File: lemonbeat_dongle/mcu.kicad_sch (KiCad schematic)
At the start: 39 parts, among them J201 USB_A, J202 Prog, J203 u.FL, SW201 SW_Push, U201 nRF52840, Y201 32MHz, Y202 32.768kHz

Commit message: dongle: re-add 32kHz crystal to BOM
Should not be needed, but may need software adaptation for Si4467 to
work with HFCLK, so easier to keep initially and remove later.
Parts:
- C203, C204, Y202: now in the parts list
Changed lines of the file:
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@@
   )
   (symbol (lib_id "Device:C") (at 151.13 60.96 90) (unit 1)
-    (in_bom no) (on_board yes)
+    (in_bom yes) (on_board yes)
     (property "Reference" "C204" (id 0) (at 151.13 57.15 90))
     (property "Value" "12pF" (id 1) (at 151.13 64.77 90))
@@
   )
   (symbol (lib_id "Device:C") (at 151.13 50.8 270) (unit 1)
-    (in_bom no) (on_board yes)
+    (in_bom yes) (on_board yes)
     (property "Reference" "C203" (id 0) (at 151.13 46.99 90))
     (property "Value" "12pF" (id 1) (at 151.13 54.61 90))
@@
   )
   (symbol (lib_id "Device:Crystal") (at 133.35 55.88 90) (unit 1)
-    (in_bom no) (on_board yes) (fields_autoplaced)
+    (in_bom yes) (on_board yes) (fields_autoplaced)
     (property "Reference" "Y202" (id 0) (at 137.16 54.6099 90)
       (effects (font (size 1.27 1.27)) (justify right))

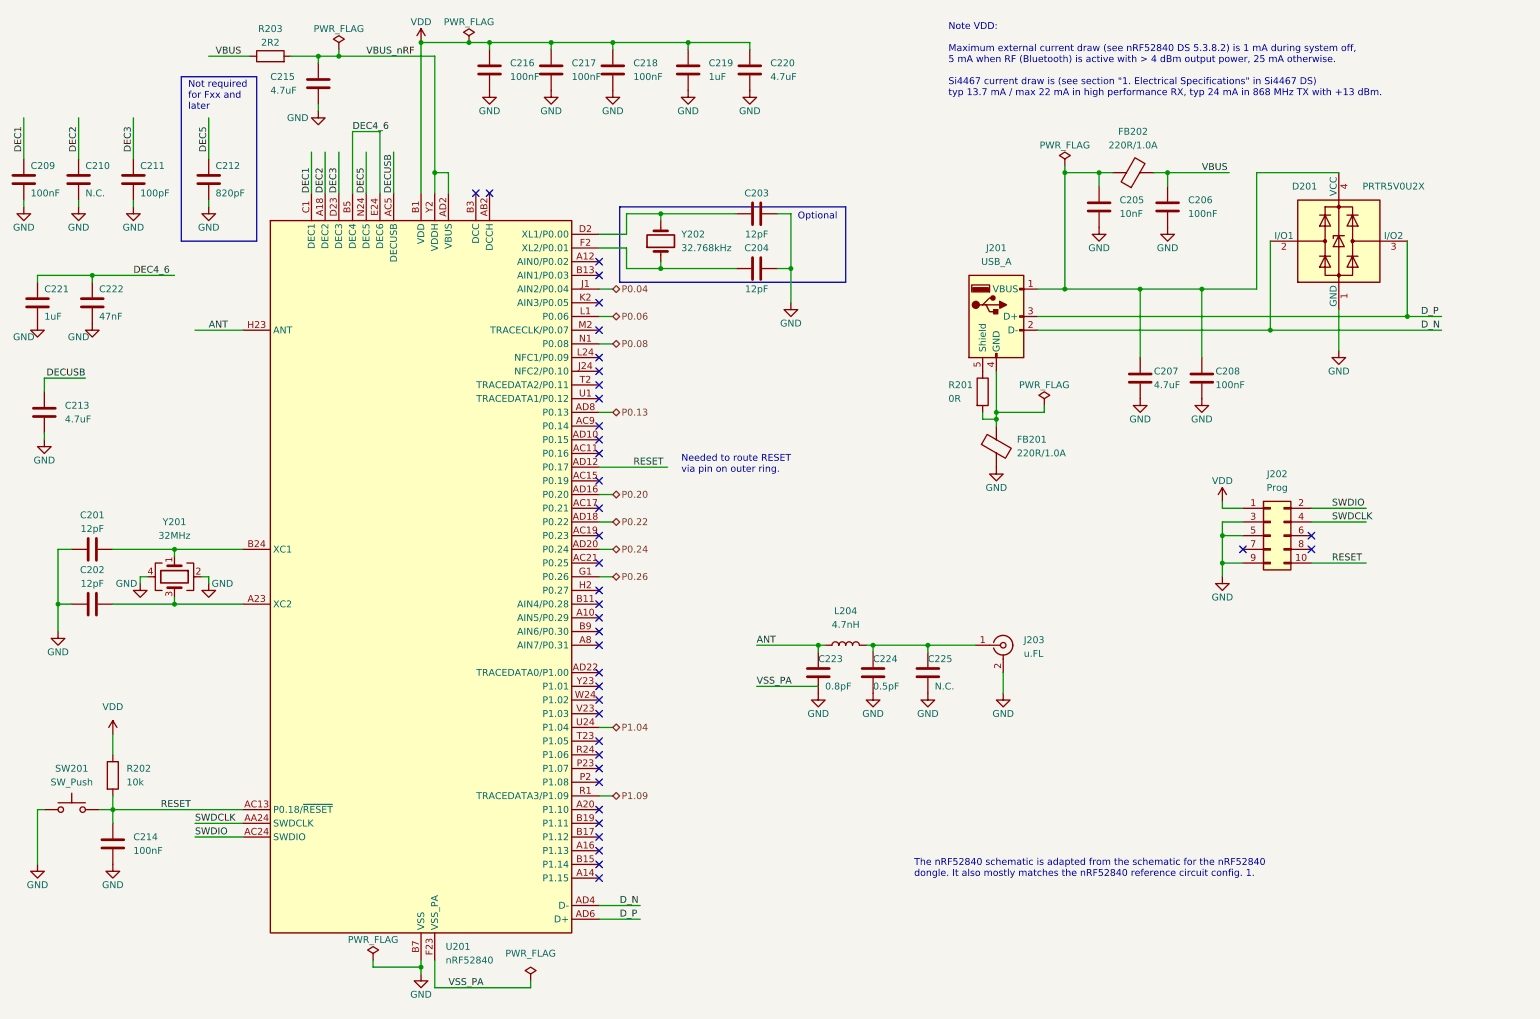
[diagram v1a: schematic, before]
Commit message: dongle: add some test points
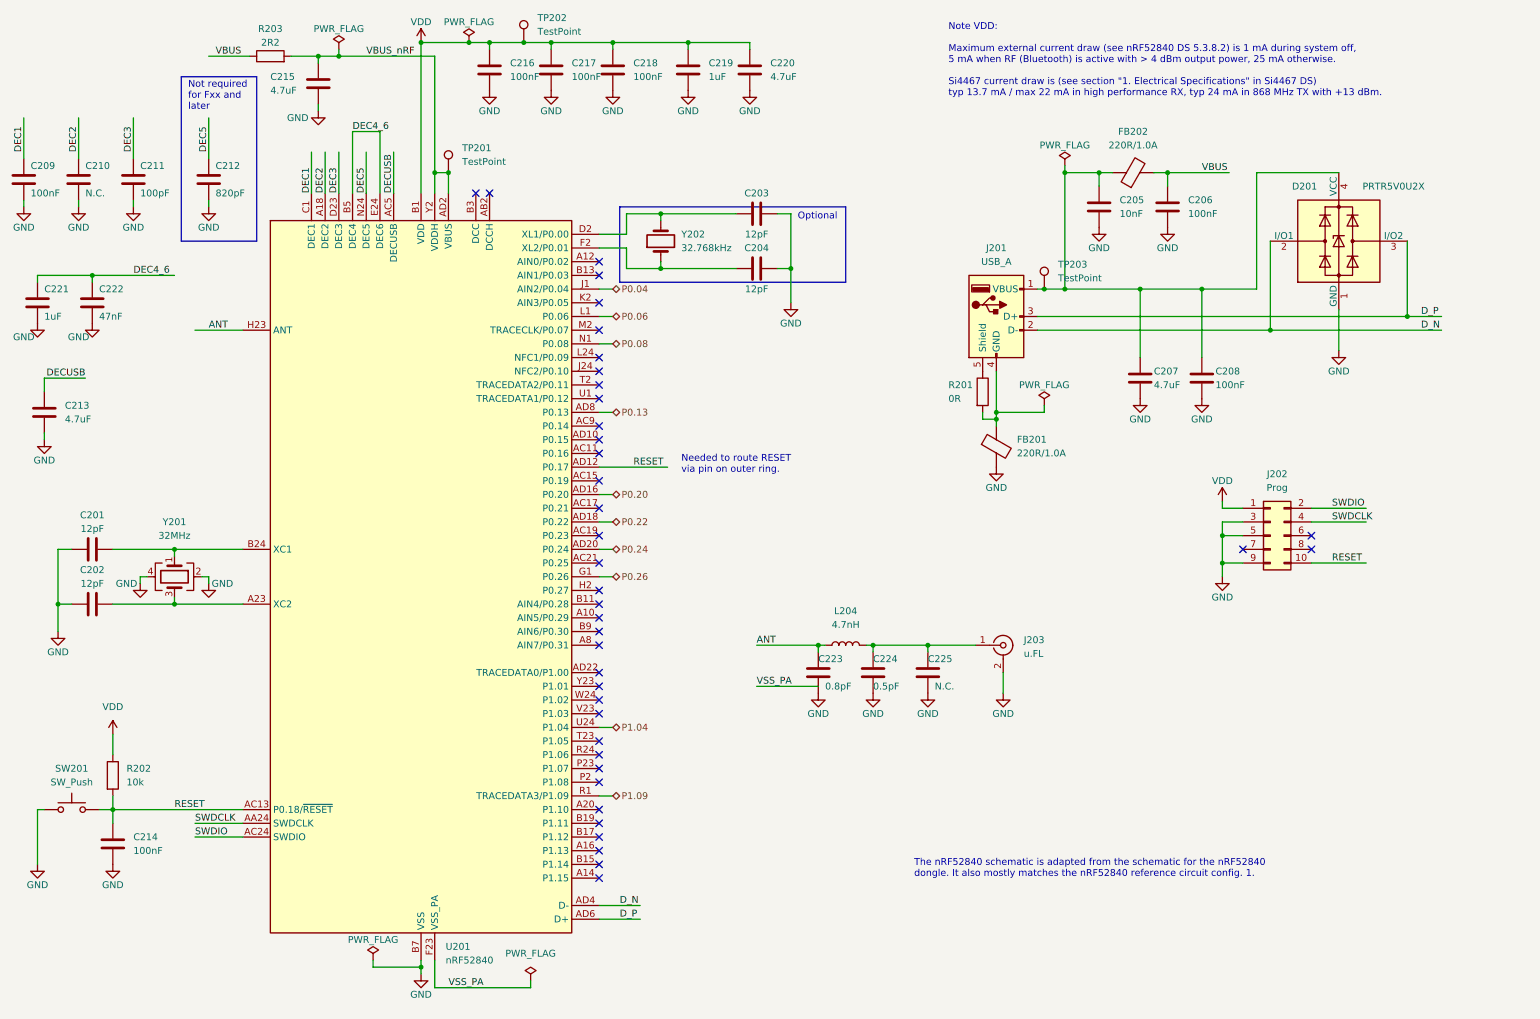
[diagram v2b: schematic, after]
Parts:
- added TP201, TP202, TP203: TestPoint, TestPoint:TestPoint_Pad_D1.0mm, symbol Connector:TestPoint
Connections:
- net VBUS_nRF: now also TP201.1
- net VDD: now also TP202.1
- net at C205.1, C207.1, C208.1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: now also TP203.1
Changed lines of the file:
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@@
   (junction (at 227.33 43.18) (diameter 0) (color 0 0 0 0)
   )
+  (junction (at 93.98 43.18) (diameter 0) (color 0 0 0 0)
+  )
   (junction (at 222.25 64.77) (diameter 0) (color 0 0 0 0)
   )
@@
   (junction (at 195.58 88.9) (diameter 0) (color 0 0 0 0)
   )
+  (junction (at 204.47 64.77) (diameter 0) (color 0 0 0 0)
+  )
   (junction (at 157.48 60.96) (diameter 0) (color 0 0 0 0)
   )
@@
   )
   (junction (at 237.49 110.49) (diameter 0) (color 0 0 0 0)
+  )
+  (junction (at 107.95 19.05) (diameter 0) (color 0 0 0 0)
   )
   (junction (at 233.68 64.77) (diameter 0) (color 0 0 0 0)
@@
     (stroke (width 0) (type default) (color 0 0 0 0))
   )
+  (wire (pts (xy 204.47 64.77) (xy 208.28 64.77))
+    (stroke (width 0) (type default) (color 0 0 0 0))
+  )
   (wire (pts (xy 182.88 130.81) (xy 182.88 132.08))
     (stroke (width 0) (type default) (color 0 0 0 0))
@@
     (stroke (width 0) (type default) (color 0 0 0 0))
   )
-  (wire (pts (xy 101.6 19.05) (xy 113.03 19.05))
+  (wire (pts (xy 101.6 19.05) (xy 107.95 19.05))
     (stroke (width 0) (type default) (color 0 0 0 0))
   )
@@
     (stroke (width 0) (type default) (color 0 0 0 0))
   )
+  (wire (pts (xy 107.95 19.05) (xy 113.03 19.05))
+    (stroke (width 0) (type default) (color 0 0 0 0))
+  )
   (wire (pts (xy 195.58 87.63) (xy 195.58 88.9))
     (stroke (width 0) (type default) (color 0 0 0 0))
@@
     (stroke (width 0) (type default) (color 0 0 0 0))
   )
-  (wire (pts (xy 203.2 64.77) (xy 208.28 64.77))
+  (wire (pts (xy 203.2 64.77) (xy 204.47 64.77))
     (stroke (width 0) (type default) (color 0 0 0 0))
   )
@@
     (effects (font (size 1.27 1.27)) (justify left bottom))
   )
-  (label "RESET" (at 40.64 161.29 0)
+  (label "RESET" (at 43.18 161.29 0)
     (effects (font (size 1.27 1.27)) (justify left bottom))
   )
@@
     (pin "1")
     (pin "2")
+  )
+  (symbol (lib_id "Connector:TestPoint") (at 107.95 19.05 0) (unit 1)
+    (in_bom yes) (on_board yes) (fields_autoplaced)
+    (property "Reference" "TP202" (id 0) (at 110.49 14.4779 0)
+      (effects (font (size 1.27 1.27)) (justify left))
+    )
+    (property "Value" "TestPoint" (id 1) (at 110.49 17.0179 0)
+      (effects (font (size 1.27 1.27)) (justify left))
+    )
+    (property "Footprint" "TestPoint:TestPoint_Pad_D1.0mm" (id 2) (at 113.03 19.05 0)
+      (effects (font (size 1.27 1.27)) hide)
+    )
+    (property "Datasheet" "~" (id 3) (at 113.03 19.05 0)
+      (effects (font (size 1.27 1.27)) hide)
+    )
+    (pin "1")
   )
   (symbol (lib_id "Device:C") (at 69.85 26.67 0) (unit 1)
@@
     (pin "2")
   )
+  (symbol (lib_id "Connector:TestPoint") (at 93.98 43.18 0) (unit 1)
+    (in_bom yes) (on_board yes) (fields_autoplaced)
+    (property "Reference" "TP201" (id 0) (at 96.52 38.6079 0)
+      (effects (font (size 1.27 1.27)) (justify left))
+    )
+    (property "Value" "TestPoint" (id 1) (at 96.52 41.1479 0)
+      (effects (font (size 1.27 1.27)) (justify left))
+    )
+    (property "Footprint" "TestPoint:TestPoint_Pad_D1.0mm" (id 2) (at 99.06 43.18 0)
+      (effects (font (size 1.27 1.27)) hide)
+    )
+    (property "Datasheet" "~" (id 3) (at 99.06 43.18 0)
+      (effects (font (size 1.27 1.27)) hide)
+    )
+    (pin "1")
+  )
   (symbol (lib_id "power:GND") (at 233.68 85.09 0) (unit 1)
     (in_bom yes) (on_board yes)
@@
       (effects (font (size 1.27 1.27)) hide)
     )
+    (pin "1")
+  )
+  (symbol (lib_id "Connector:TestPoint") (at 204.47 64.77 0) (unit 1)
+    (in_bom yes) (on_board yes) (fields_autoplaced)
+    (property "Reference" "TP203" (id 0) (at 207.01 60.1979 0)
+      (effects (font (size 1.27 1.27)) (justify left))
+    )
+    (property "Value" "TestPoint" (id 1) (at 207.01 62.7379 0)
+      (effects (font (size 1.27 1.27)) (justify left))
+    )
+    (property "Footprint" "TestPoint:TestPoint_Pad_D1.0mm" (id 2) (at 209.55 64.77 0)
+      (effects (font (size 1.27 1.27)) hide)
+    )
+    (property "Datasheet" "~" (id 3) (at 209.55 64.77 0)
+      (effects (font (size 1.27 1.27)) hide)
+    )

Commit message: dongle: schematic: notes & cosmetic changes
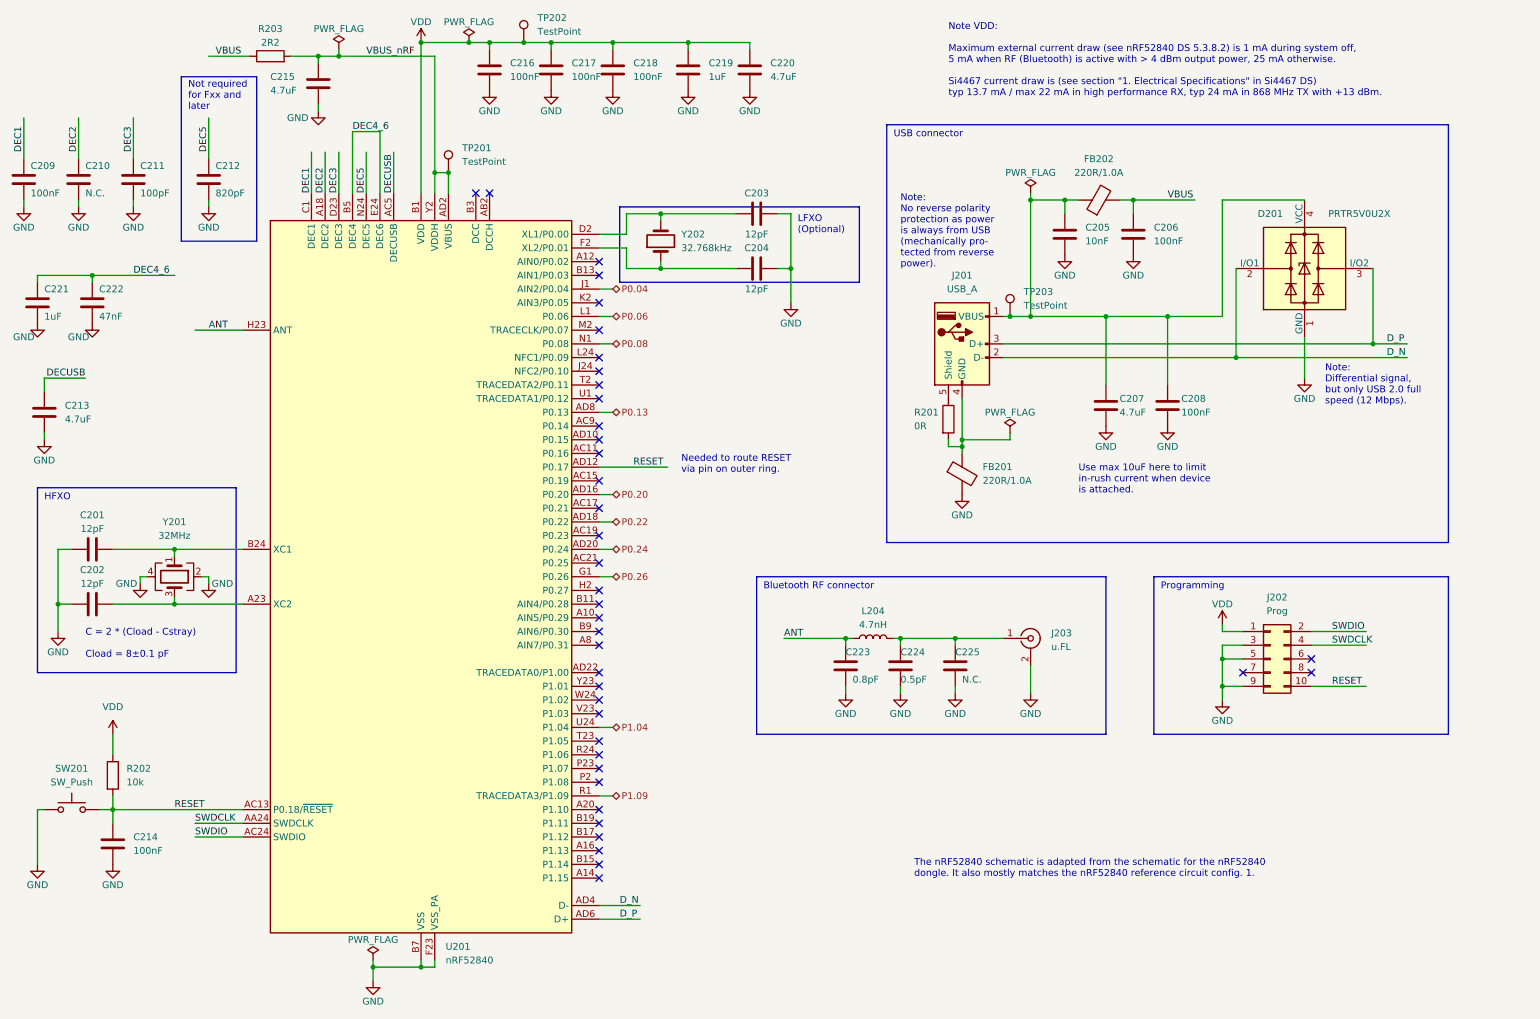
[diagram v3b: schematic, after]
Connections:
- net VSS_PA is gone; now on net GND: U201.F23 (VSS_PA)
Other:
- note added: "Bluetooth RF connector"
- note added: "C = 2 * (Cload - Cstray) Cload = 8±0.1 pF"
- note added: "HFXO"
- note added: "LFXO (Optional)"
- note added: "Note: Differential signal, but only USB 2.0 full speed (12 Mbps)."
- note added: "Note: No reverse polarity protection as power is always from USB (mechanically pro- tected from reverse power)."
- note added: "Programming"
- note added: "USB connector"
- note added: "Use max 10uF here to limit in-rush current when device is attached."
- note removed: "Optional"
- moved on the sheet: C205, C206, C207, C208, C223, C224, C225, D201, FB201, FB202, J201, J202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

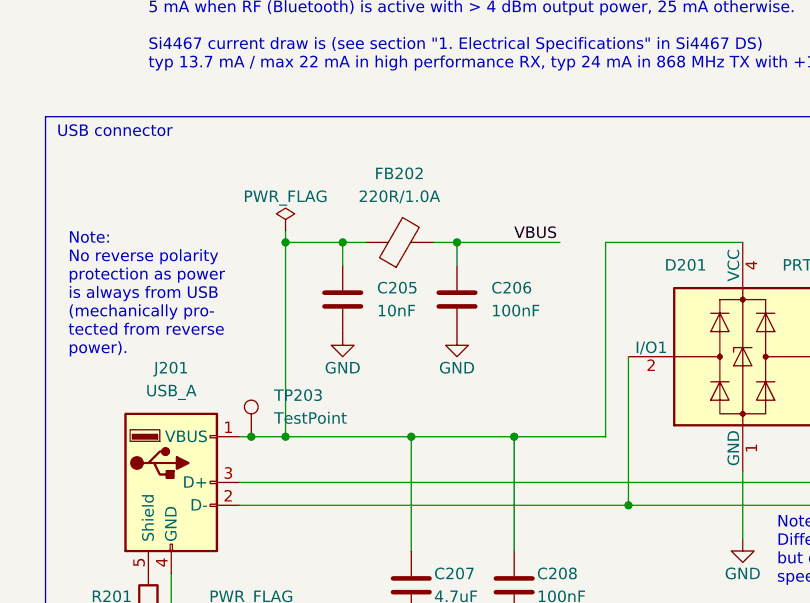
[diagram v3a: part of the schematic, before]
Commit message: dongle: schematic: add fuse
Add a 100 mA fuse for USB power supply. This is somewhat optional as
the host side should also have a fuse, but nice since the host-side
fuse will have a higher current rating and we're not allowed to draw
more than 100 mA without previous negotiation according to the USB
specification.
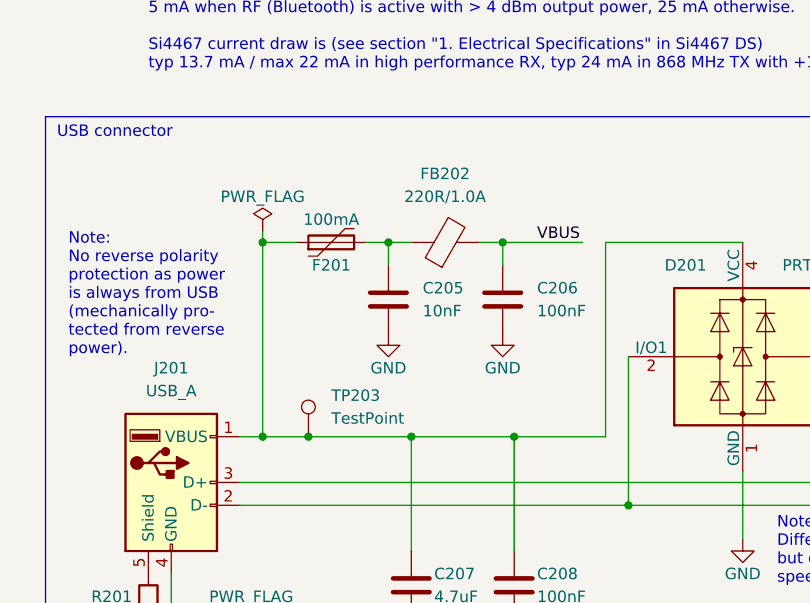
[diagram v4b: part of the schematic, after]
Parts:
- added F201: 100mA, Fuse:Fuse_0603_1608Metric, symbol Device:Polyfuse
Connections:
- net at C207.1, C208.1, D201.4 (VCC)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: now also F201.1; no longer C205.1, FB202.1
- new net: C205.1, F201.2, FB202.1
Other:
- moved on the sheet: C205, C206, FB202, TP203
